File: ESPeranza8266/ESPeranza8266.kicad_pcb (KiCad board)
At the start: 2 copper layers, 22.9 x 30.5 mm, 91 parts, among them J1 GS1, J11 Conn_01x10_Male, J12 Conn_01x04, J13 Conn_01x04, J14 Conn_01x02, J15 Conn_01x03, J16 Conn_01x02, J17 Conn_01x02, J18 Conn_01x01_Male, J3 GS3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

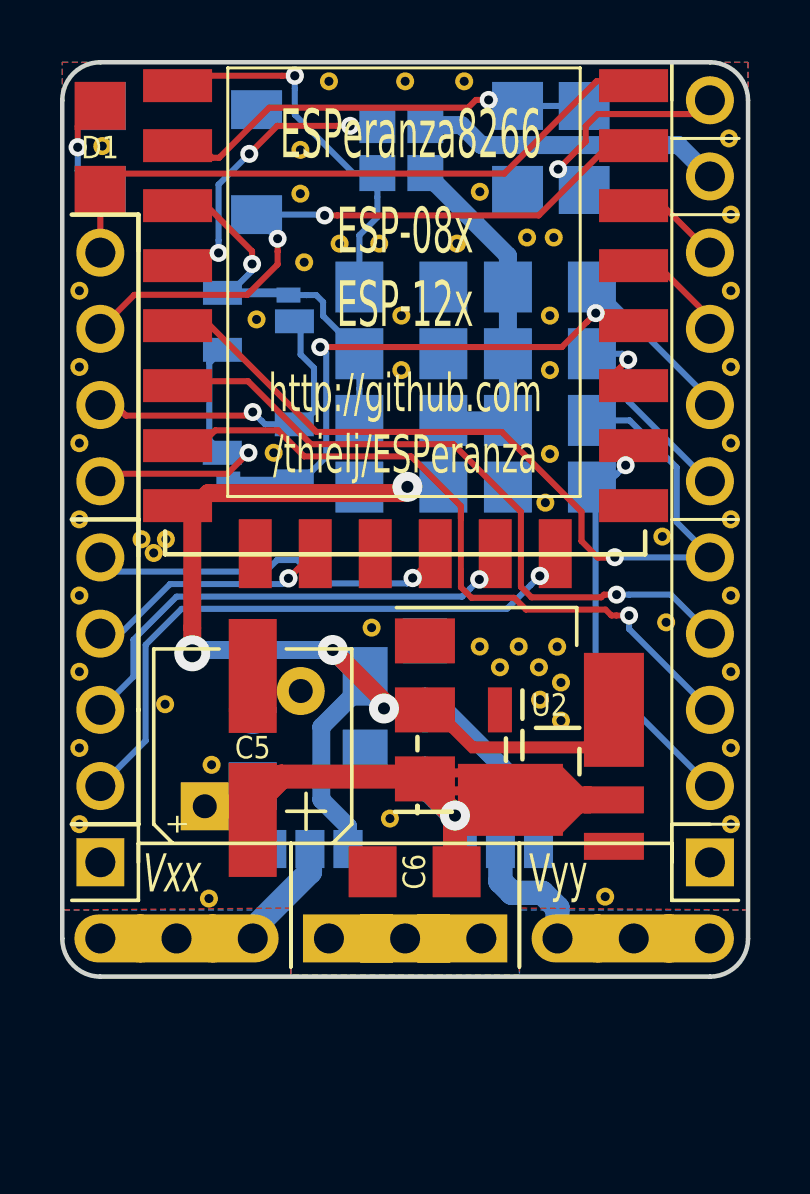
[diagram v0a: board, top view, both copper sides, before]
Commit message: added RXD (D9) to jumper J1 changed fontsizes and placements of component references
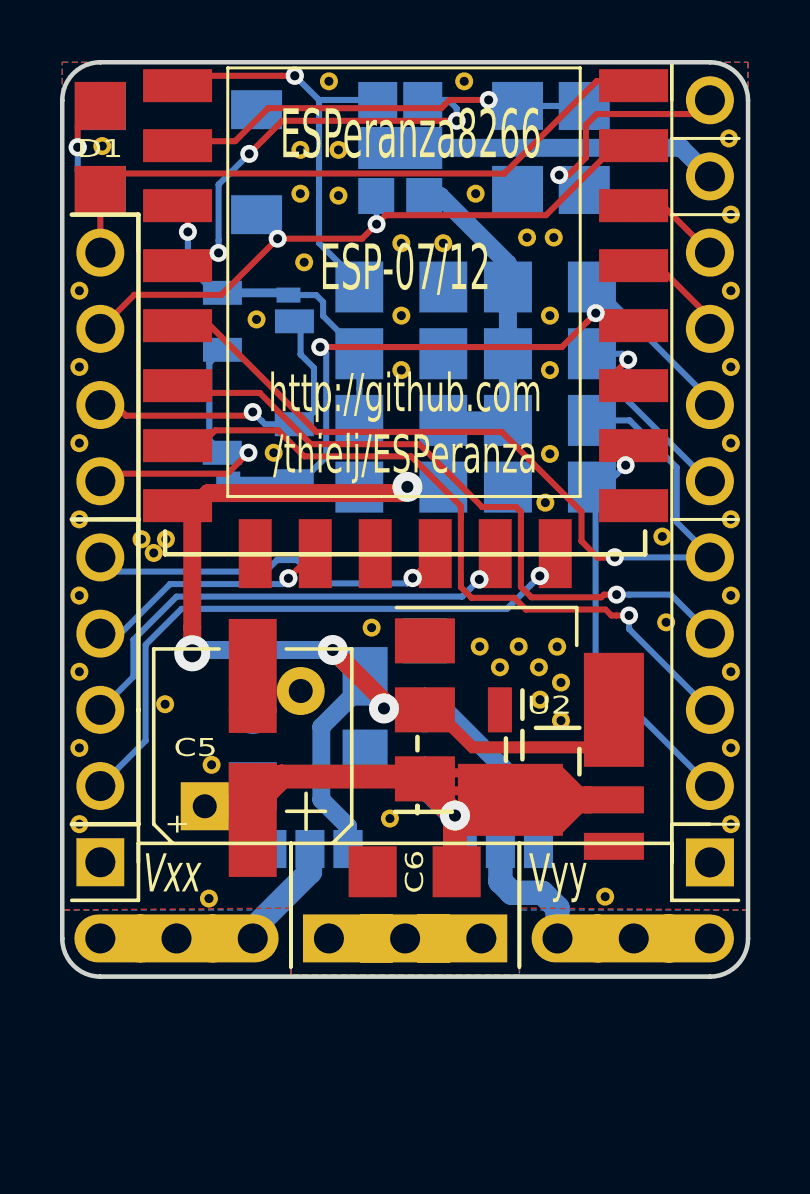
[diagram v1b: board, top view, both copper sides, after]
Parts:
- removed the VIA** at (86.4, 47.6)
- removed the VIA** at (85.5, 53.0)
- removed the VIA** at (84.2, 53.0)
- added VIA**: VIA-0.6mm, PERSONAL:VIA-0.6mm, F.Cu at (86.2, 53.0)
- added VIA**: VIA-0.6mm, PERSONAL:VIA-0.6mm, F.Cu at (84.1, 51.4)
- added VIA**: VIA-0.6mm, PERSONAL:VIA-0.6mm, F.Cu at (84.1, 49.9)
- moved J1 0.76 mm to (86.2, 50.6)
- moved VIA** 0.46 mm to (87.6, 53.0)
- moved VIA** 0.15 mm to (88.7, 51.4)
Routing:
- net /IO16: track 9.32 -> 13.6 mm
- net /RST: track 12.7 -> 13.7 mm
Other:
- net class 12 mil: clearance 0.2032 -> 0.2
- net class 16 mil / 8 mil: clearance 0.2032 -> 0.2
- net class 24 mil / 12 mil: clearance 0.2032 -> 0.2
- net class 32 mil / 12 mil: clearance 0.2032 -> 0.2
- net class Default: clearance 0.2032 -> 0.2; trace_width 0.2032 -> 0.2
- rule trace_clearance: 0.2032 -> 0.2
- board text added: "ESP-07/12"
- board text added: "v0.9.5"
- board text removed: "ESP-08x ESP-12x"
- board text removed: "v0.9.2"

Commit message: Added MCP73831 (battery charge management controller) and battery connector
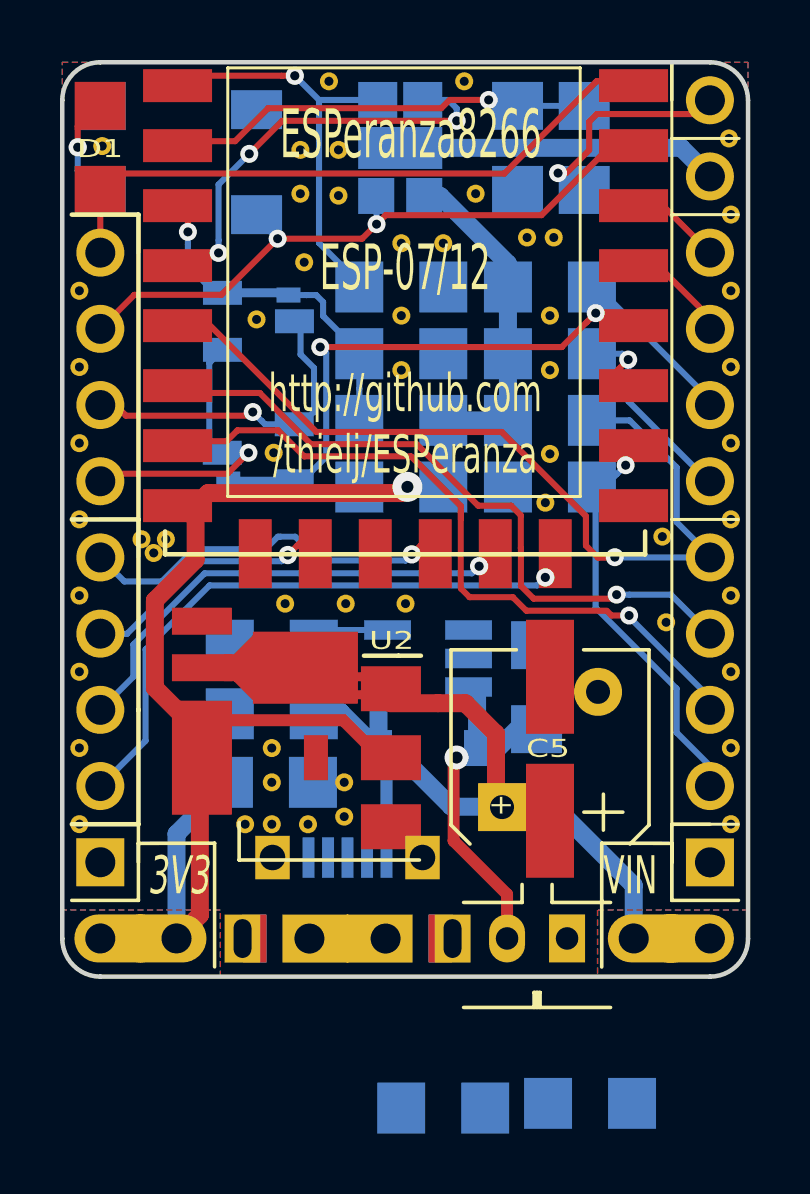
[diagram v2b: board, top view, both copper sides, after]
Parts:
- removed J15: Conn_01x03, PERSONAL:GroundPad_01x03
- removed J3: GS3, Connectors:GS3
- removed J4: GS4, Connectors:GS3
- removed the VIA** at (85.9, 72.2)
- removed the VIA** at (79.8, 74.9)
- removed the VIA** at (93.0, 74.8)
- removed the VIA** at (91.4, 66.5)
- removed the VIA** at (89.5, 67.2)
- removed the VIA** at (88.8, 66.5)
- removed the VIA** at (90.1, 66.5)
- removed the VIA** at (90.8, 67.2)
- removed the VIA** at (90.9, 68.2)
- removed the VIA** at (85.2, 65.8)
- removed the VIA** at (91.6, 68.9)
- removed the VIA** at (91.6, 67.7)
- removed VR**: AMS1117-BOTTOM-PADS, AMS1117+BOTTOM-PADS
- added C7: 4.7uF, PERSONAL:SMD_1206_0805_Universal, B.Cu at (90.7, 67.8)
- added D3: Yellow, PERSONAL:SMD_1206_0805_Universal, B.Cu at (92.5, 81.7)
- added D4: MBR120, Diodes_SMD:D_SOD-123, B.Cu at (87.1, 69.8)
- added J10: USB_OTG, Connectors_USB:USB_Micro-B_Molex-105017-0001, B.Cu at (84.4, 75.8)
- added J19: LiPo, Connectors_JST:JST_PH_B2B-PH-K_02x2.00mm_Straight, F.Cu at (89.8, 76.2)
- added R10: 2.0k, PERSONAL:SMD_1206_0805_Universal, B.Cu at (81.9, 66.4)
- added R9: 200, PERSONAL:SMD_1206_0805_Universal, B.Cu at (87.6, 81.9)
- added U3: MCP73831, TO_SOT_Packages_SMD:SOT-23-5_HandSoldering, B.Cu at (87.1, 66.9)
- added VIA**: VIA-0.6mm, PERSONAL:VIA-0.6mm, F.Cu at (81.9, 69.8)
- added VIA**: VIA-0.6mm, PERSONAL:VIA-0.6mm, F.Cu at (81.0, 72.4)
- added VIA**: VIA-0.6mm, PERSONAL:VIA-0.6mm, F.Cu at (84.3, 71.0)
- added VIA**: VIA-0.6mm, PERSONAL:VIA-0.6mm, F.Cu at (81.9, 71.0)
- added VIA**: VIA-0.6mm, PERSONAL:VIA-0.6mm, F.Cu at (84.3, 72.1)
- added VIA**: VIA-0.6mm, PERSONAL:VIA-0.6mm, F.Cu at (83.1, 72.4)
- added VIA**: VIA-0.6mm, PERSONAL:VIA-0.6mm, F.Cu at (81.9, 72.4)
- added VIA**: VIA-0.6mm, PERSONAL:VIA-0.6mm, F.Cu at (86.4, 65.0)
- C6: moved to B.Cu
- moved REF** 9.91 mm to (91.2, 71.1)
- moved C5 9.91 mm to (91.2, 69.9)
- moved U2 7.60 mm to (82.7, 70.2), turned to 180 degrees
- moved C6 7.10 mm to (81.9, 68.7)
- moved VIA** 6.99 mm to (84.4, 65.0)
- moved VIA** 5.22 mm to (82.4, 65.0)
- moved C4 3.81 mm to (81.9, 71.0), turned to 0 degrees
- moved J16 2.54 mm to (94.0, 76.2)
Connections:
- J14 pad 1: /Vxx -> +3V3
- J14 pad 2: /Vxx -> +3V3
- J16 pad 1: /Vyy -> VDC
- J16 pad 2: /Vyy -> VDC
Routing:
- net /Vyy: track 11.9 -> 0.00 mm
- net +BATT: track 0.00 -> 11.8 mm, vias 0 -> 1
- net +3V3: track 54.1 -> 43.0 mm, vias 4 -> 1
- net /Vxx: track 8.85 -> 0.00 mm
- net VDC: track 22.8 -> 26.8 mm, vias 1 -> 0
- net /PROG: track 0.00 -> 2.67 mm
- net /ADC: track 14.7 -> 13.6 mm
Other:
- board text added: "3V3"
- board text added: "CC·BY·SA"
- board text added: "DX"
- board text added: "VIN"
- board text added: "v0.99"
- board text removed: "8266"
- board text removed: "CC-BY-SA"
- board text removed: "ESPeranza"
- board text removed: "Vxx"
- board text removed: "Vyy"
- board text removed: "XX"
- board text removed: "v0.9.5"
